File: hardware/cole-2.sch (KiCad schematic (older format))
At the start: 0 parts

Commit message: Partial updates for hardware revision 2
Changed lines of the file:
@@
 EESchema Schematic File Version 4
-EELAYER 26 0
+LIBS:cole-2-cache
+EELAYER 30 0
 EELAYER END
 $Descr A4 11693 8268
 encoding utf-8
-Sheet 1 5
+Sheet 1 6
 Title ""
 Date ""
@@
 S 2050 1550 2550 1850
 U 5B7D0B8D
-F0 "CPU Logic" 50
+F0 "Core Logic" 50
 F1 "cpu.sch" 50
 $EndSheet
@@
 S 2050 4000 2500 1750
 U 5B9337AE
-F0 "I/O" 39
-F1 "io.sch" 39
+F0 "VIA and SPI" 39
+F1 "via.sch" 39
 $EndSheet
 $Sheet
 S 6650 4000 2500 1700
 U 5C1871C9
-F0 "Clock and Reset" 50
-F1 "clocka_and_reset.sch" 50
+F0 "VGA" 50
+F1 "vga.sch" 50
+$EndSheet
+$Sheet
+S 2050 6250 2500 1350
+U 5D58F4B4
+F0 "Serial Ports" 50
+F1 "serial.sch" 50
 $EndSheet
 $EndSCHEMATC

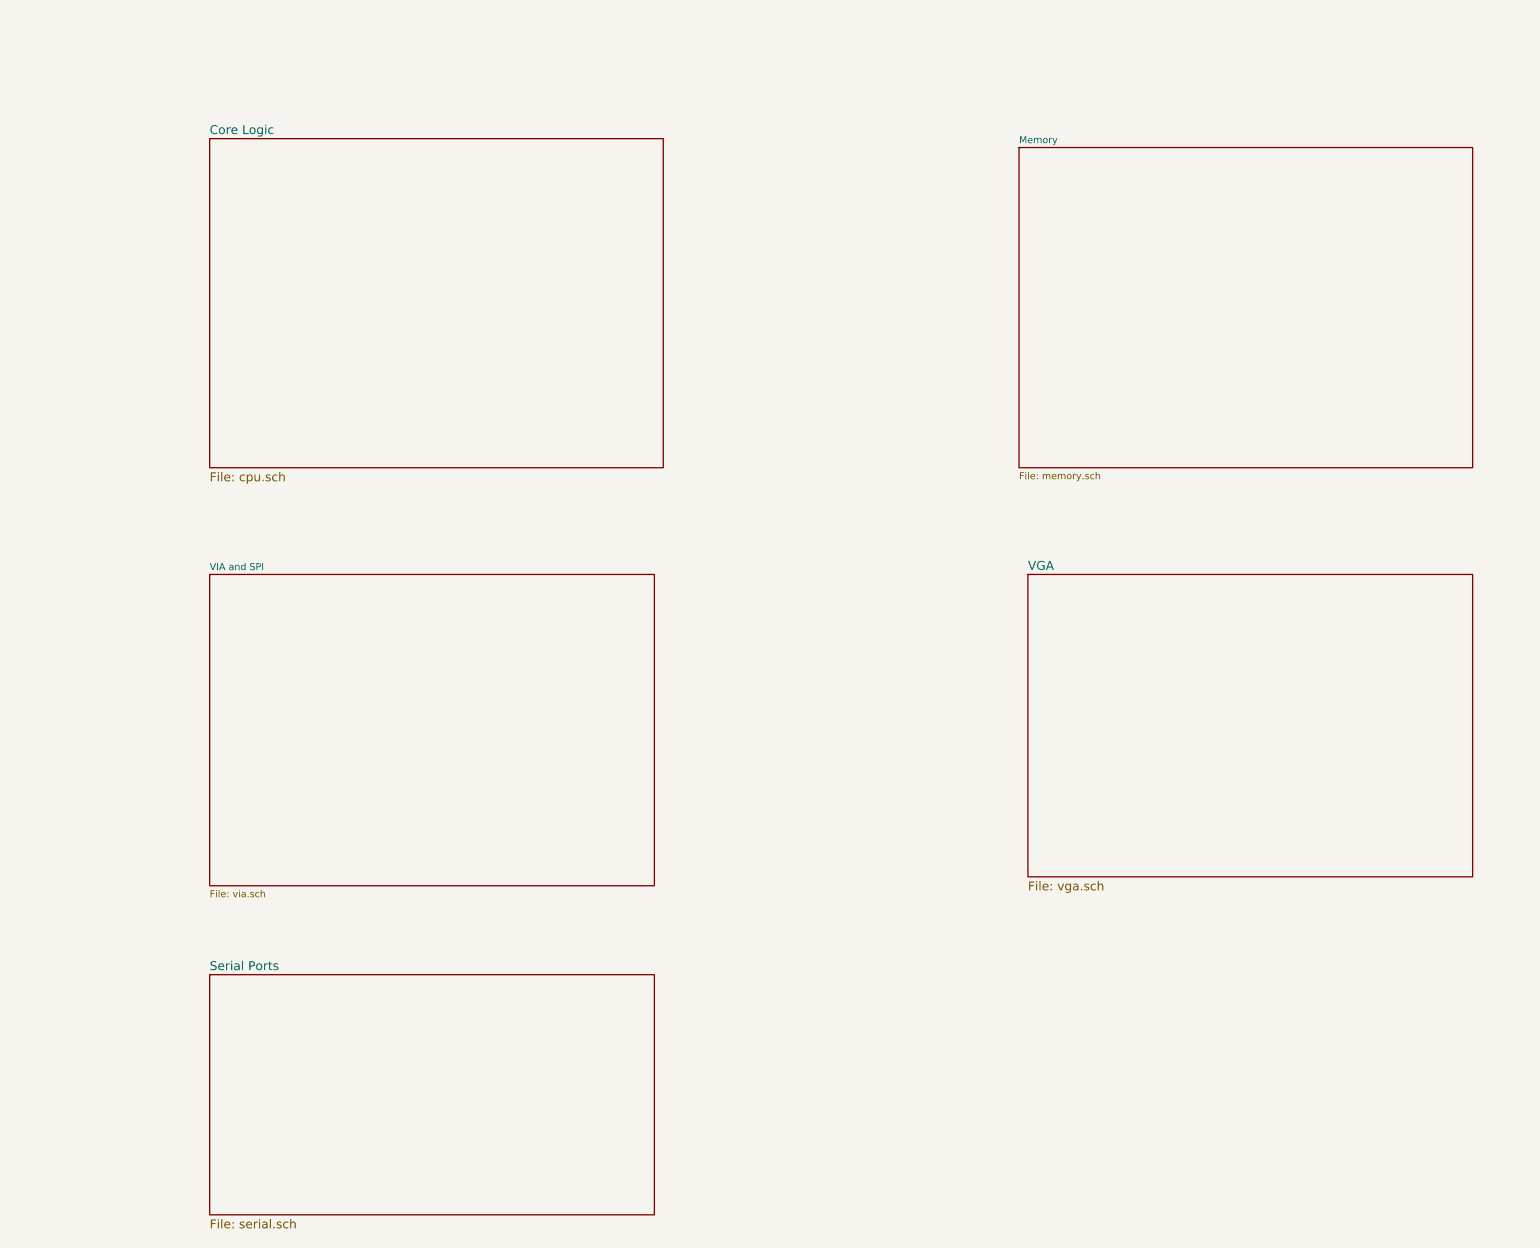
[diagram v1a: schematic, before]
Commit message: Add SPI and missing caps on MAX3232s.
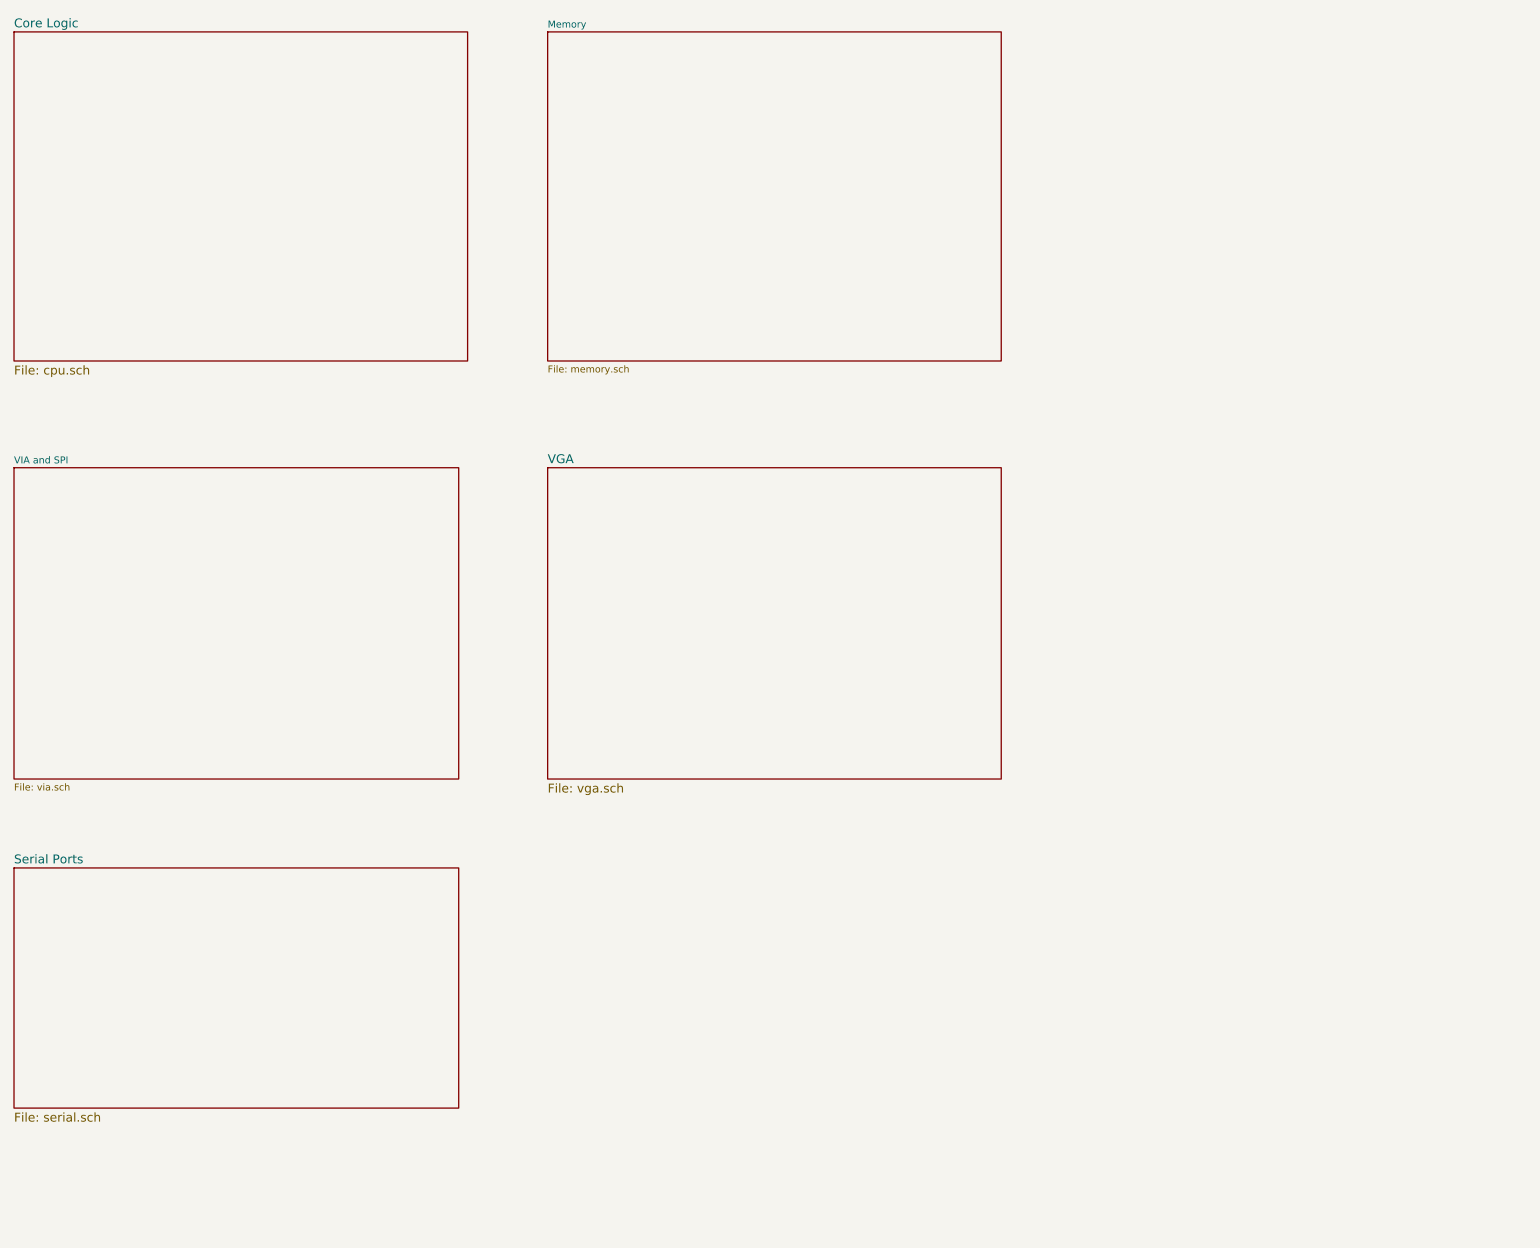
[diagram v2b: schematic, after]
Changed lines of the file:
@@
 encoding utf-8
 Sheet 1 6
-Title ""
+Title "COLE-2 Single Board Computer"
 Date ""
-Rev ""
+Rev "2"
 Comp ""
 Comment1 ""
@@
 $EndDescr
 $Sheet
-S 2050 1550 2550 1850
+S 950  950  2550 1850
 U 5B7D0B8D
 F0 "Core Logic" 50
@@
 $EndSheet
 $Sheet
-S 6600 1600 2550 1800
+S 3950 950  2550 1850
 U 5B877537
 F0 "Memory" 39
@@
 $EndSheet
 $Sheet
-S 2050 4000 2500 1750
+S 950  3400 2500 1750
 U 5B9337AE
 F0 "VIA and SPI" 39
@@
 $EndSheet
 $Sheet
-S 6650 4000 2500 1700
+S 3950 3400 2550 1750
 U 5C1871C9
 F0 "VGA" 50
@@
 $EndSheet
 $Sheet
-S 2050 6250 2500 1350
+S 950  5650 2500 1350
 U 5D58F4B4
 F0 "Serial Ports" 50

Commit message: Combine VIA, SPI, and UART into a single io.sch sheet. The serial.sch sheet is now just the serial ports and the line drivers.
Add ports.sch sheet for remaining I/O ports.
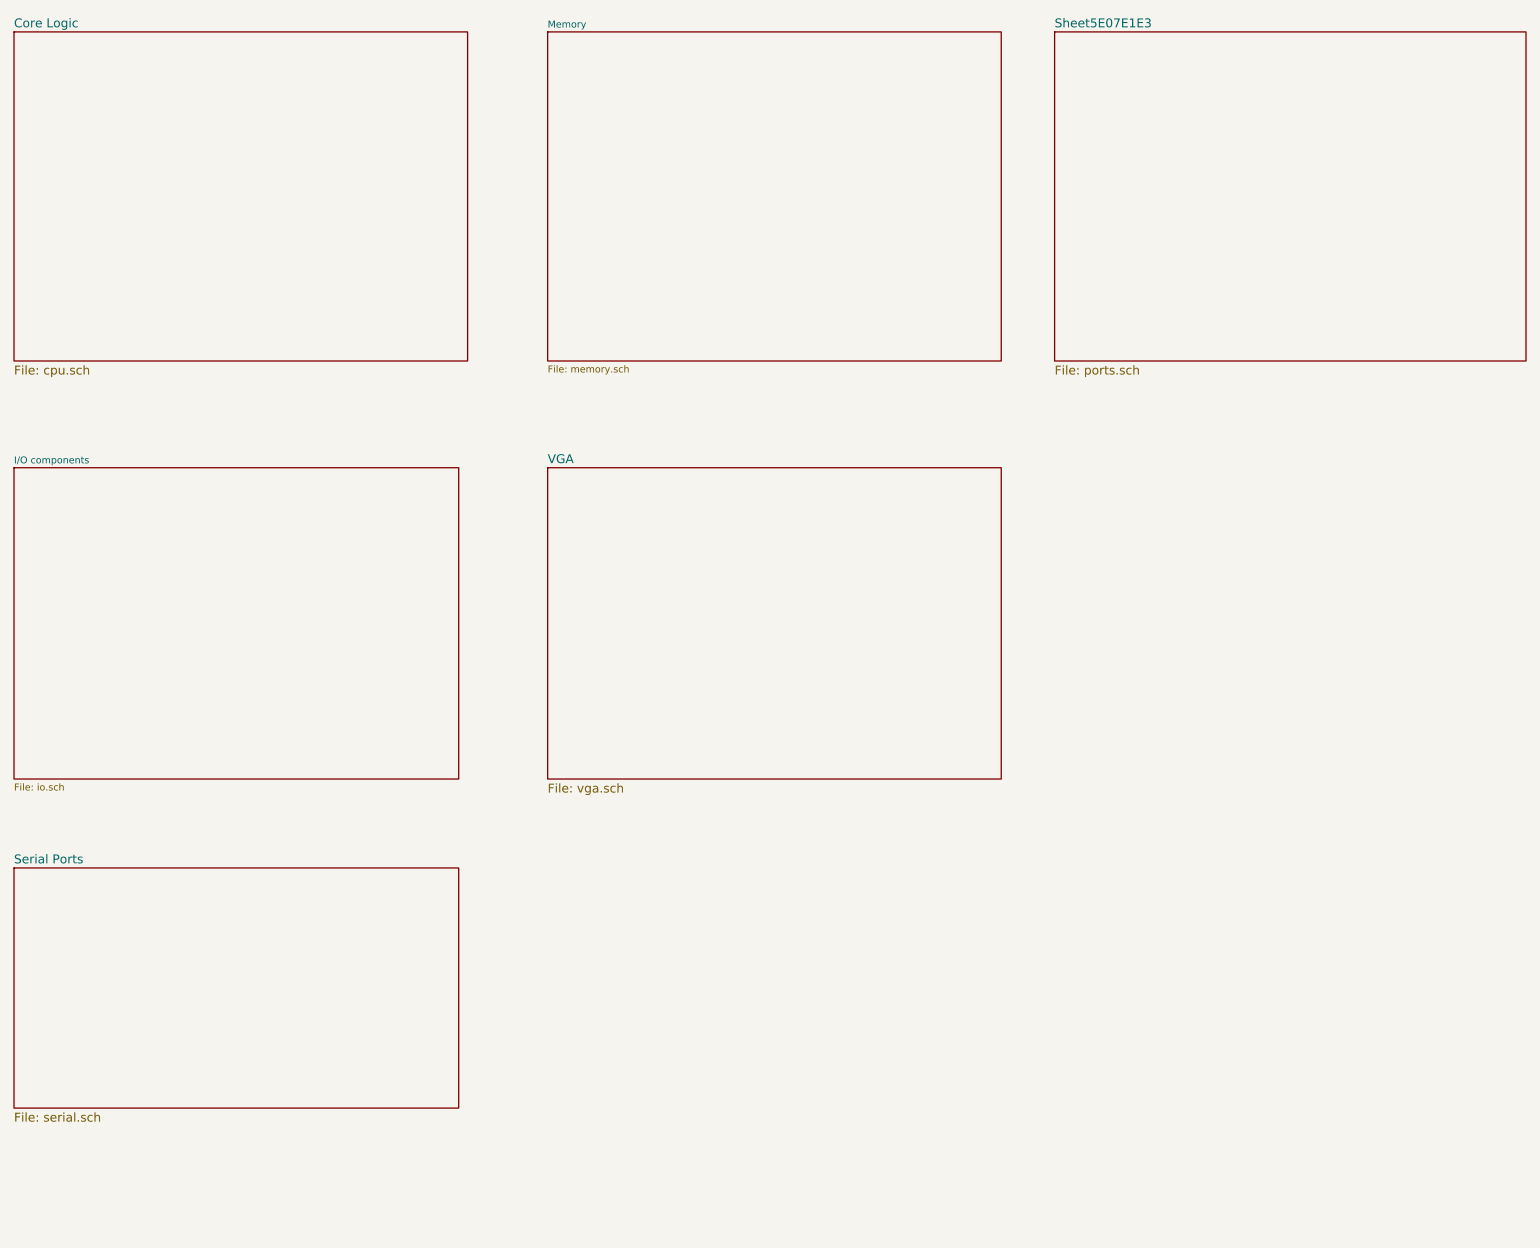
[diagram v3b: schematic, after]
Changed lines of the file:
@@
 $Descr A4 11693 8268
 encoding utf-8
-Sheet 1 6
+Sheet 1 7
 Title "COLE-2 Single Board Computer"
 Date ""
@@
 S 950  3400 2500 1750
 U 5B9337AE
-F0 "VIA and SPI" 39
-F1 "via.sch" 39
+F0 "I/O components" 39
+F1 "io.sch" 39
 $EndSheet
 $Sheet
@@
 F1 "serial.sch" 50
 $EndSheet
+$Sheet
+S 6800 950  2650 1850
+U 5E07E1E4
+F0 "Sheet5E07E1E3" 50
+F1 "ports.sch" 50
+$EndSheet
 $EndSCHEMATC

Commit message: Latest schematic
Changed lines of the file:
@@
 $Descr A4 11693 8268
 encoding utf-8
-Sheet 1 7
+Sheet 1 8
 Title "COLE-2 Single Board Computer"
 Date ""
@@
 F1 "ports.sch" 50
 $EndSheet
+$Sheet
+S 6850 3400 2550 1700
+U 5E0D032F
+F0 "Sheet5E0D032E" 50
+F1 "input_devices.sch" 50
+$EndSheet
 $EndSCHEMATC
